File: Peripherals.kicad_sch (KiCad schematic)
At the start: 37 parts, among them J8 Conn_01x05, SW1 SW_Push, SW2 SW_Push, SW3 SW_Push, SW4 SW_Push, SW5 SW_SPDT, SW6 SW_SPDT, SW7 SW_SPDT, SW8 SW_SPDT, SW9 SW_SPDT

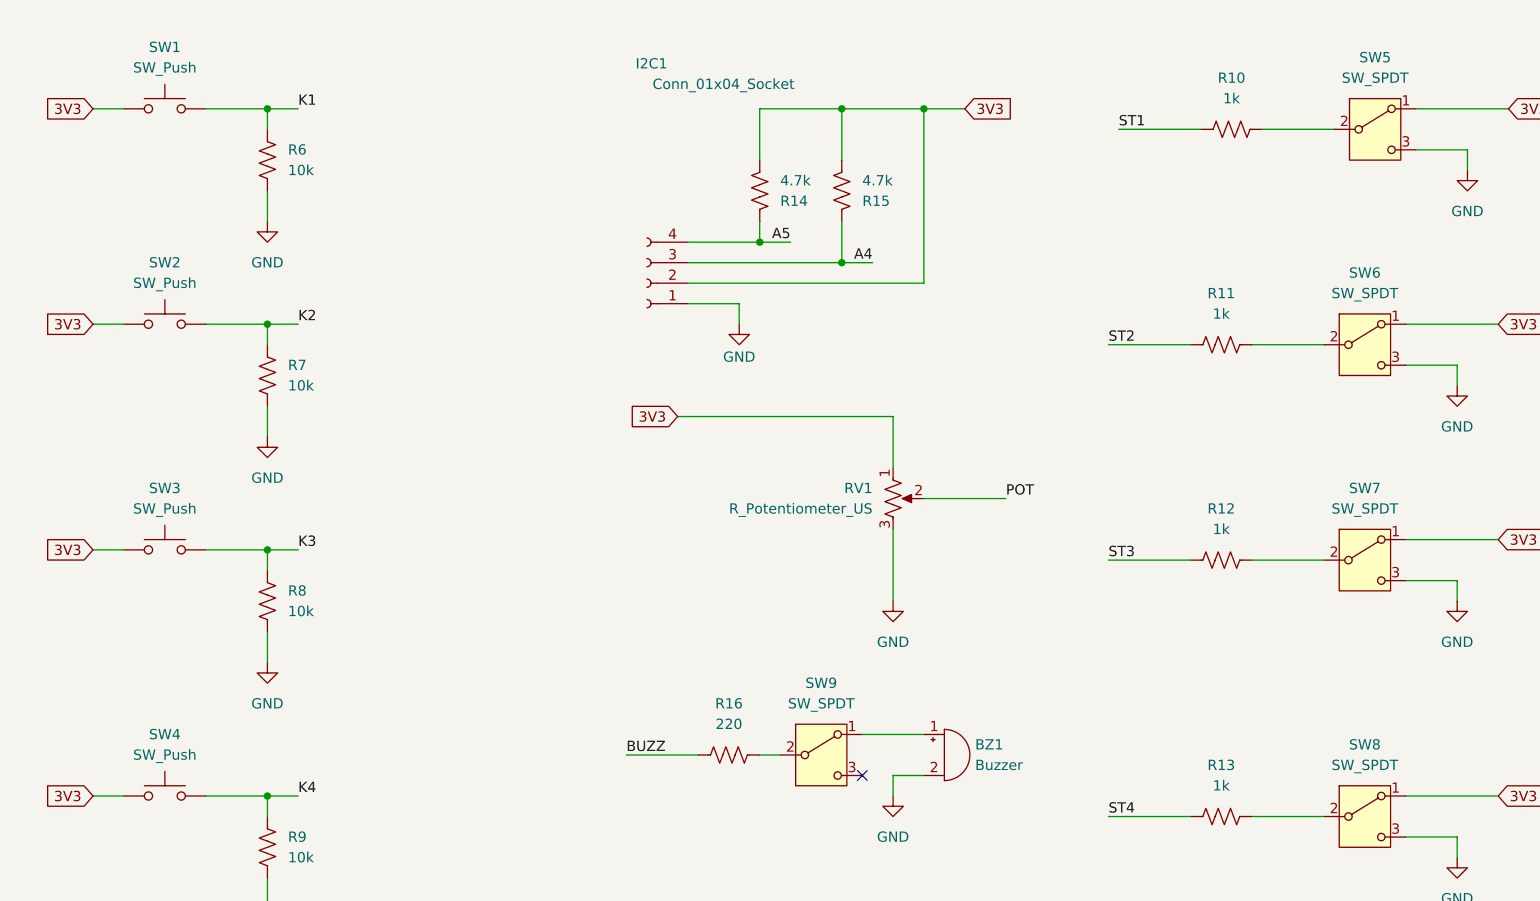
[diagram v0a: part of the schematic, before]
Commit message: - added global nets for A4 and A5
- I2C connetor changes
- Throw swtiches and button identifiers changed

Signed-off-by: deyviaa <legoked@gmail.com>
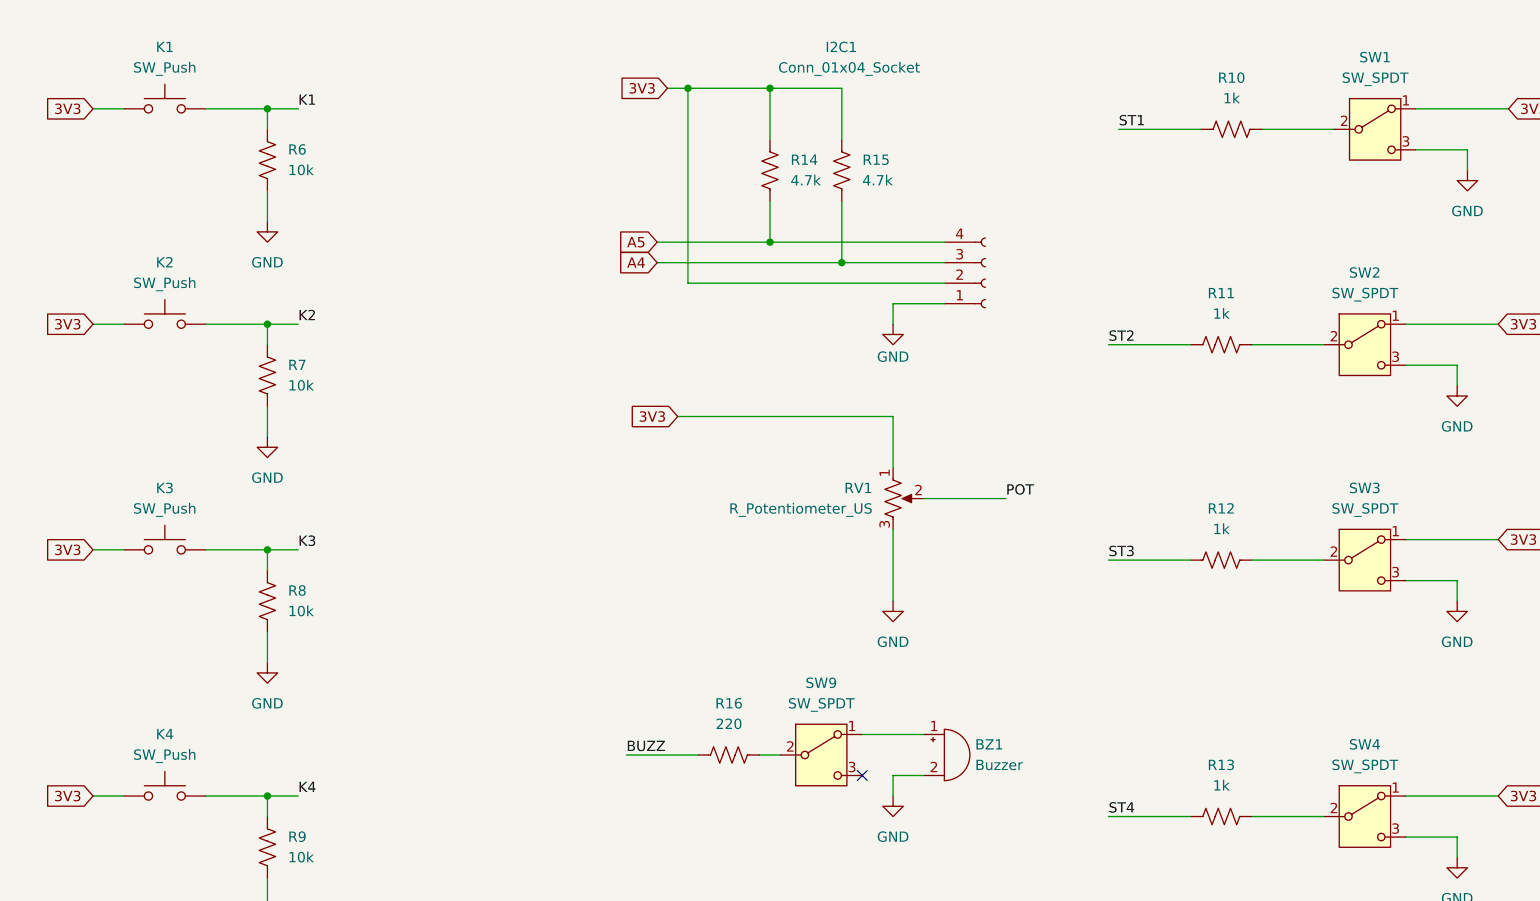
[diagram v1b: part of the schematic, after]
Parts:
- renumbered SW1 to K1, SW2 to K2, SW3 to K3, SW4 to K4, SW5 to SW1, SW6 to SW2, SW7 to SW3, SW8 to SW4
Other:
- moved on the sheet: I2C1, R14, R15
